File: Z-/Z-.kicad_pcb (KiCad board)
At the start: 4 copper layers, 98 x 98 mm, 142 parts, among them J1 200528-0100, J2 U.FL, J3 U.FL, J5 Conn_01x02, K1 IM11DGR, Q1 NX3008NBKS, Q10 MBT2222ADW1T1, Q11 NX3008NBKS, Q12 MBT2222ADW1T1, Q15 IRFTS9342PBF, Q17 IRFTS9342PBF, Q19 IRFTS9342PBF, Q2 MBT2222ADW1T1, Q20 IRLML2803, Q21 SiRA99DP, Q3 NX3008NBKS, Q4 MBT2222ADW1T1, Q5 NX3008NBKS, Q6 MBT2222ADW1T1, Q7 NX3008NBKS, Q8 MBT2222ADW1T1, Q9 NX3008NBKS, U1 OPT4003DNPRQ1, U2 PCA9633DP2, U4 DRV8235RTER, U5 USBLC6-2P6

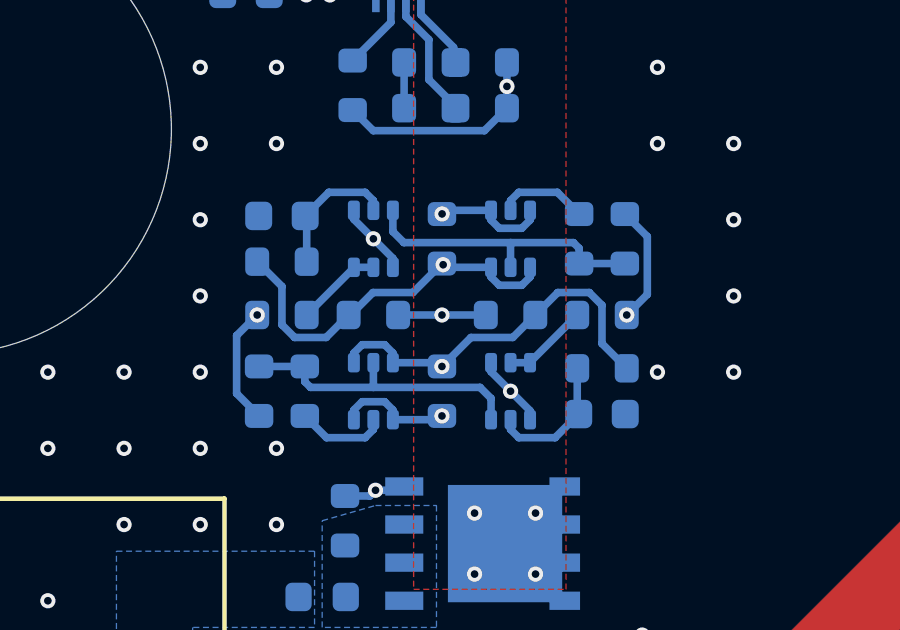
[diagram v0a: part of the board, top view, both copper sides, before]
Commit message: Fixed silkscreen
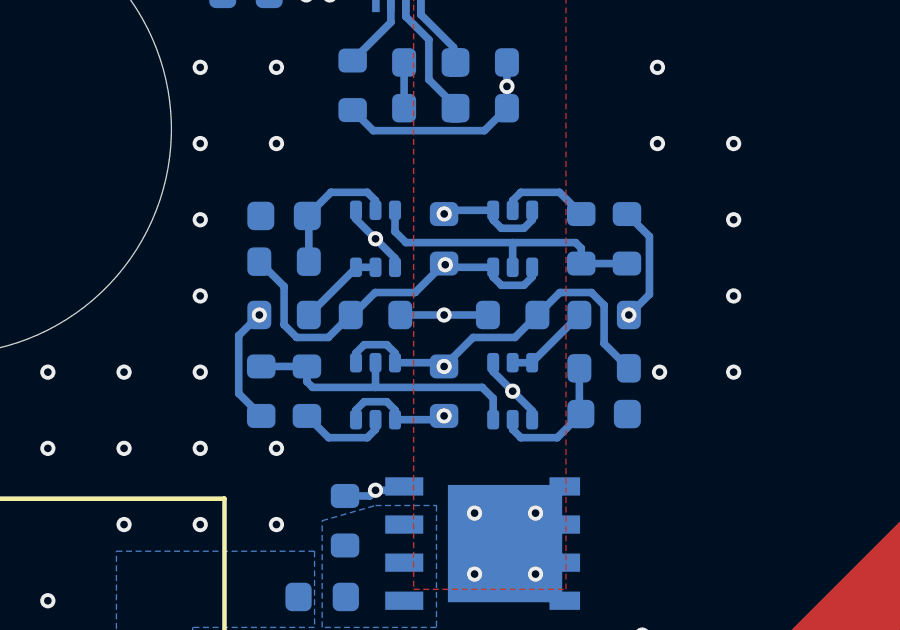
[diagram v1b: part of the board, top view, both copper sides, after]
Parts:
- moved C11 0.07 mm to (163.6, 98.6)
- moved C6 0.07 mm to (174.2, 105.2)
- moved Q10 0.07 mm to (166.6, 104.4)
- moved Q11 0.07 mm to (166.6, 99.3)
- moved Q12 0.07 mm to (171.2, 99.3)
- moved Q9 0.07 mm to (171.2, 104.4)
- moved R40 0.07 mm to (164.3, 104.4)
- moved R42 0.07 mm to (174.2, 101.9)
- moved R45 0.07 mm to (168.9, 104.4)
- moved R46 0.07 mm to (162.8, 104.4)
- moved R50 0.07 mm to (171.2, 101.9)
- moved R52 0.07 mm to (174.2, 103.6)
- moved R54 0.07 mm to (173.5, 99.3)
- moved R56 0.07 mm to (163.6, 101.9)
- moved R57 0.07 mm to (168.9, 99.3)
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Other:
- board text added: "ARGUS Cubesat Carnegie Mellon University Z- Solar Panel v3"
- board text added: "CDR_EN"
- board text added: "M3V3"
- board text added: "P3V3"
- board text removed: "3.3V"
- board text removed: "ARGUS-1 Cubesat Carnegie Mellon University Z- Solar Panel v2"
